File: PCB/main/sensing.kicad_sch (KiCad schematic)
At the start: 6 parts

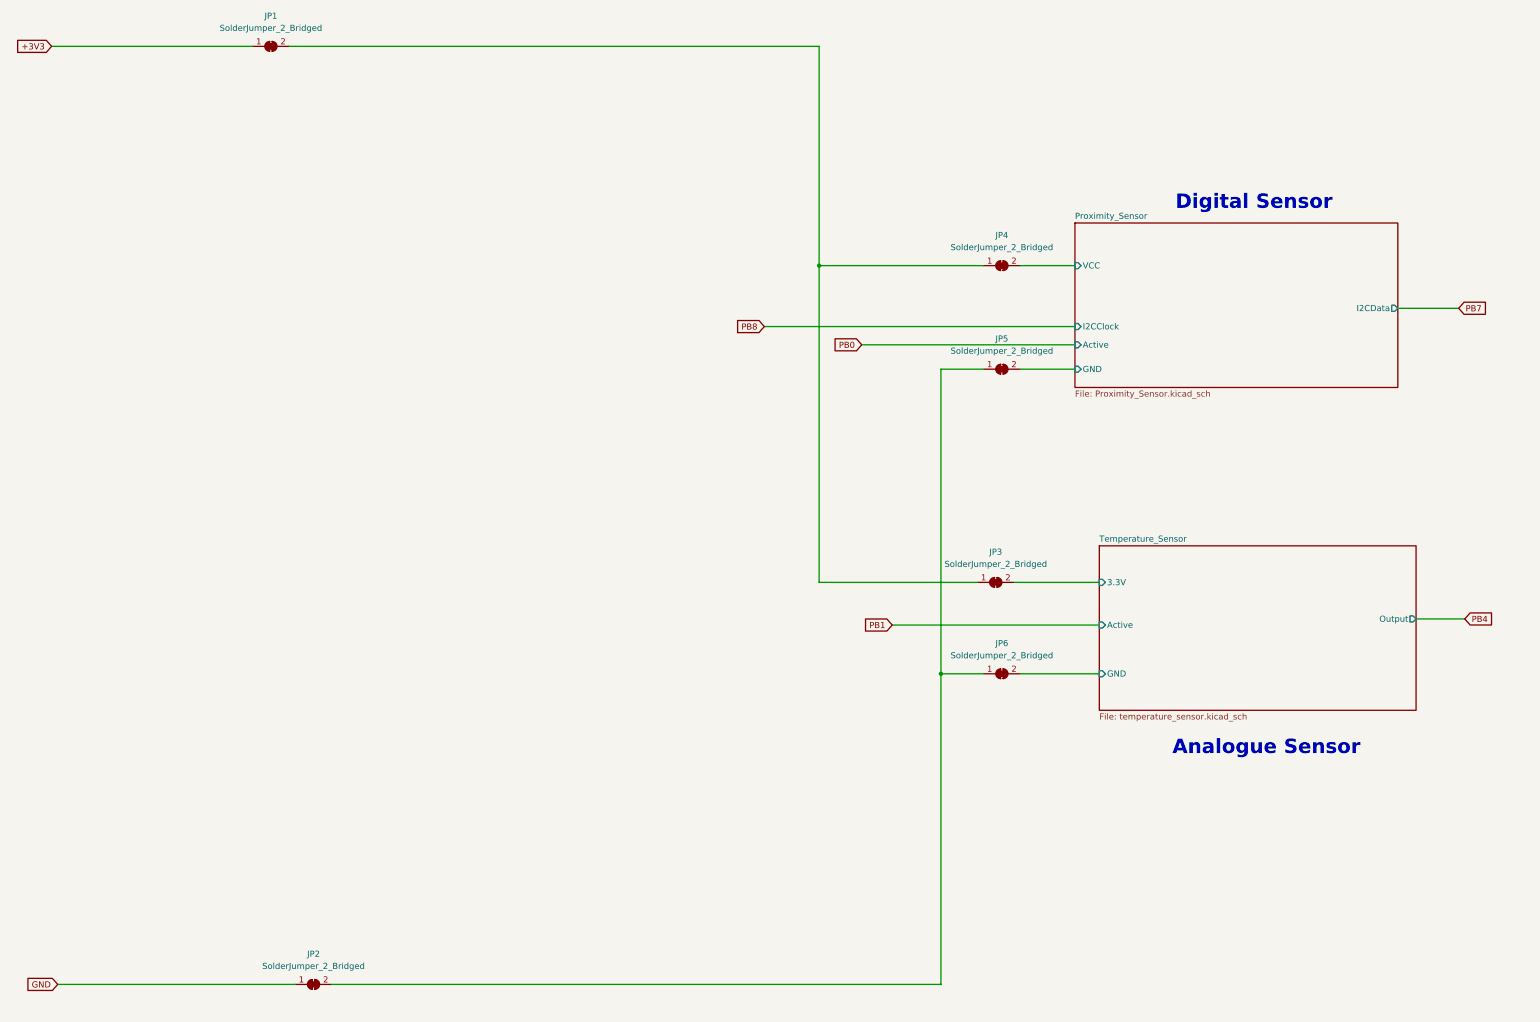
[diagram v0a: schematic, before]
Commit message: Correct labels
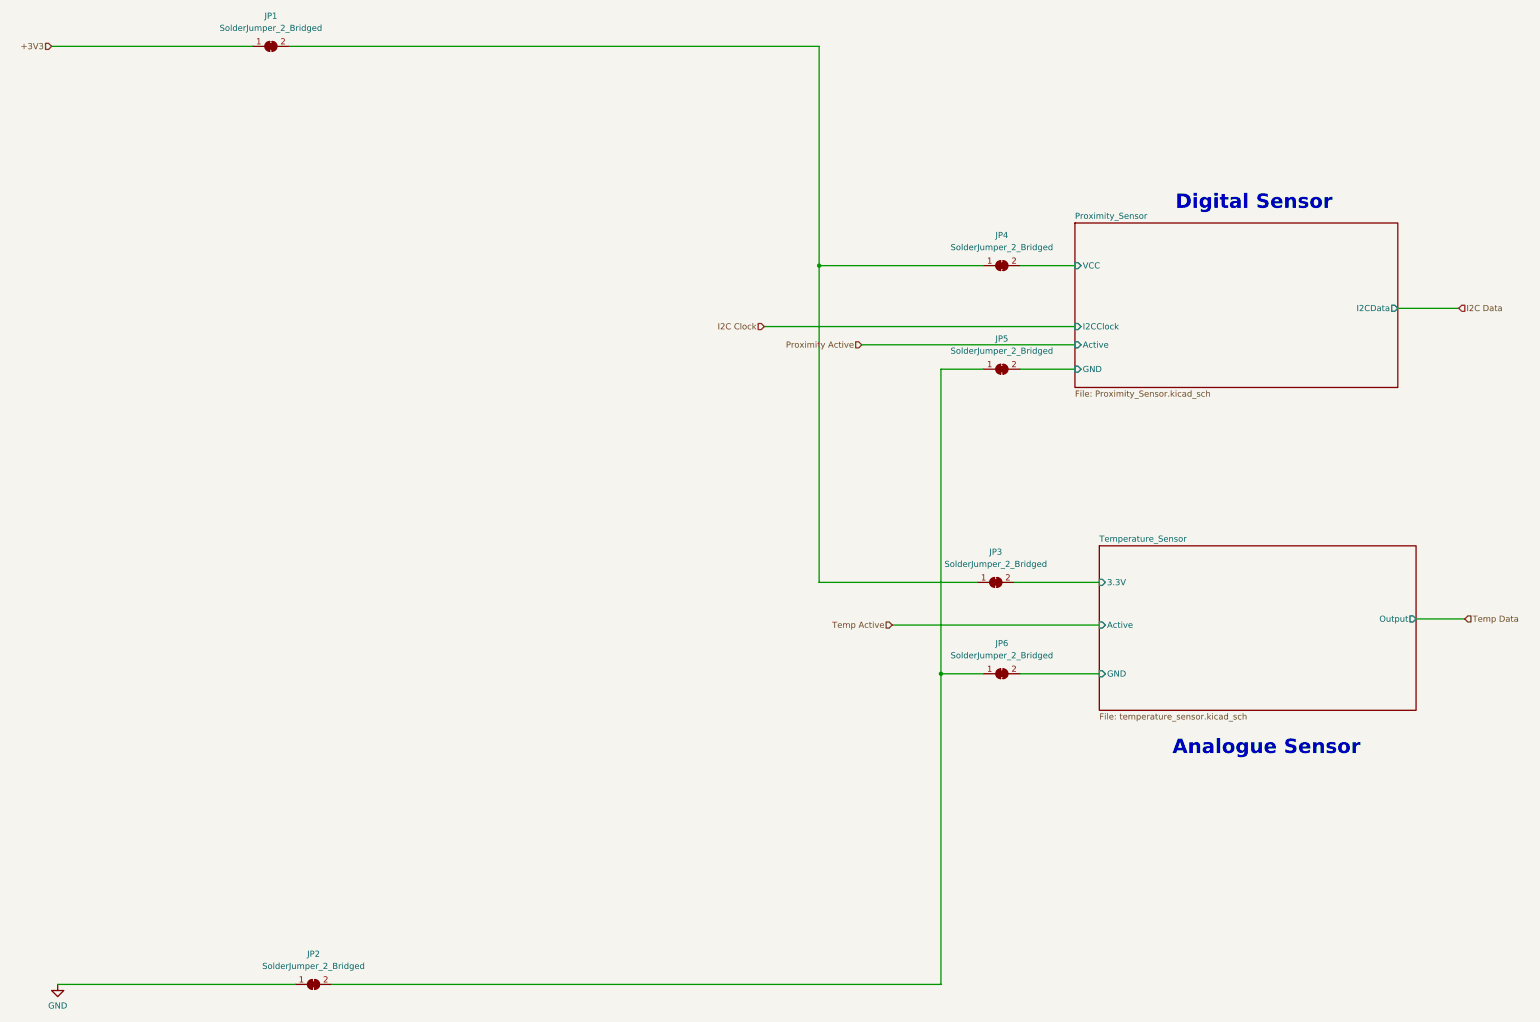
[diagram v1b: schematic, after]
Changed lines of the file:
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@@
     (effects (font (size 3 3) (thickness 0.6) bold) (justify left bottom))
   )
-  (global_label "PB8" (shape input) (at 185.42 105.41 180) (fields_autoplaced)
+  (hierarchical_label "Temp Data" (shape input) (at 331.47 166.37 0)
+    (effects (font (size 1.27 1.27)) (justify left))
+  )
+  (hierarchical_label "I2C Clock" (shape input) (at 185.42 105.41 180)
     (effects (font (size 1.27 1.27)) (justify right))
-    (property "Intersheet References" "${INTERSHEET_REFS}" (id 0) (at 179.2574 105.3306 0)
-      (effects (font (size 1.27 1.27)) (justify right) hide)
+  )
+  (hierarchical_label "Temp Active" (shape input) (at 212.09 167.64 180)
+    (effects (font (size 1.27 1.27)) (justify right))
+  )
+  (hierarchical_label "Proximity Active" (shape input) (at 205.74 109.22 180)
+    (effects (font (size 1.27 1.27)) (justify right))
+  )
+  (hierarchical_label "I2C Data" (shape input) (at 330.2 101.6 0)
+    (effects (font (size 1.27 1.27)) (justify left))
+  )
+  (hierarchical_label "+3V3" (shape input) (at 36.83 46.99 180)
+    (effects (font (size 1.27 1.27)) (justify right))
+  )
+  (symbol (lib_id "power:GND") (at 38.1 242.57 0) (unit 1)
+    (in_bom yes) (on_board yes) (fields_autoplaced)
+    (property "Reference" "#PWR024" (id 0) (at 38.1 248.92 0)
+      (effects (font (size 1.27 1.27)) hide)
     )
-  )
-  (global_label "PB7" (shape input) (at 330.2 101.6 0) (fields_autoplaced)
-    (effects (font (size 1.27 1.27)) (justify left))
-    (property "Intersheet References" "${INTERSHEET_REFS}" (id 0) (at 336.3626 101.5206 0)
-      (effects (font (size 1.27 1.27)) (justify left) hide)
+    (property "Value" "GND" (id 1) (at 38.1 247.0134 0))
+    (property "Footprint" "" (id 2) (at 38.1 242.57 0)
+      (effects (font (size 1.27 1.27)) hide)
     )
-  )
-  (global_label "+3V3" (shape input) (at 36.83 46.99 180) (fields_autoplaced)
-    (effects (font (size 1.27 1.27)) (justify right))
-    (property "Intersheet References" "${INTERSHEET_REFS}" (id 0) (at 29.3369 46.9106 0)
-      (effects (font (size 1.27 1.27)) (justify right) hide)
+    (property "Datasheet" "" (id 3) (at 38.1 242.57 0)
+      (effects (font (size 1.27 1.27)) hide)
     )
-  )
-  (global_label "GND" (shape input) (at 38.1 242.57 180) (fields_autoplaced)
-    (effects (font (size 1.27 1.27)) (justify right))
-    (property "Intersheet References" "${INTERSHEET_REFS}" (id 0) (at 31.8164 242.4906 0)
-      (effects (font (size 1.27 1.27)) (justify right) hide)
-    )
-  )
-  (global_label "PB4" (shape input) (at 331.47 166.37 0) (fields_autoplaced)
-    (effects (font (size 1.27 1.27)) (justify left))
-    (property "Intersheet References" "${INTERSHEET_REFS}" (id 0) (at 337.6326 166.2906 0)
-      (effects (font (size 1.27 1.27)) (justify left) hide)
-    )
-  )
-  (global_label "PB0" (shape input) (at 205.74 109.22 180) (fields_autoplaced)
-    (effects (font (size 1.27 1.27)) (justify right))
-    (property "Intersheet References" "${INTERSHEET_REFS}" (id 0) (at 199.5774 109.2994 0)
-      (effects (font (size 1.27 1.27)) (justify right) hide)
-    )
-  )
-  (global_label "PB1" (shape input) (at 212.09 167.64 180) (fields_autoplaced)
-    (effects (font (size 1.27 1.27)) (justify right))
-    (property "Intersheet References" "${INTERSHEET_REFS}" (id 0) (at 205.9274 167.7194 0)
-      (effects (font (size 1.27 1.27)) (justify right) hide)
-    )
+    (pin "1")
   )
   (symbol (lib_id "Jumper:SolderJumper_2_Bridged") (at 234.95 92.71 0) (unit 1)

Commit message: Work on reducing ERC flags
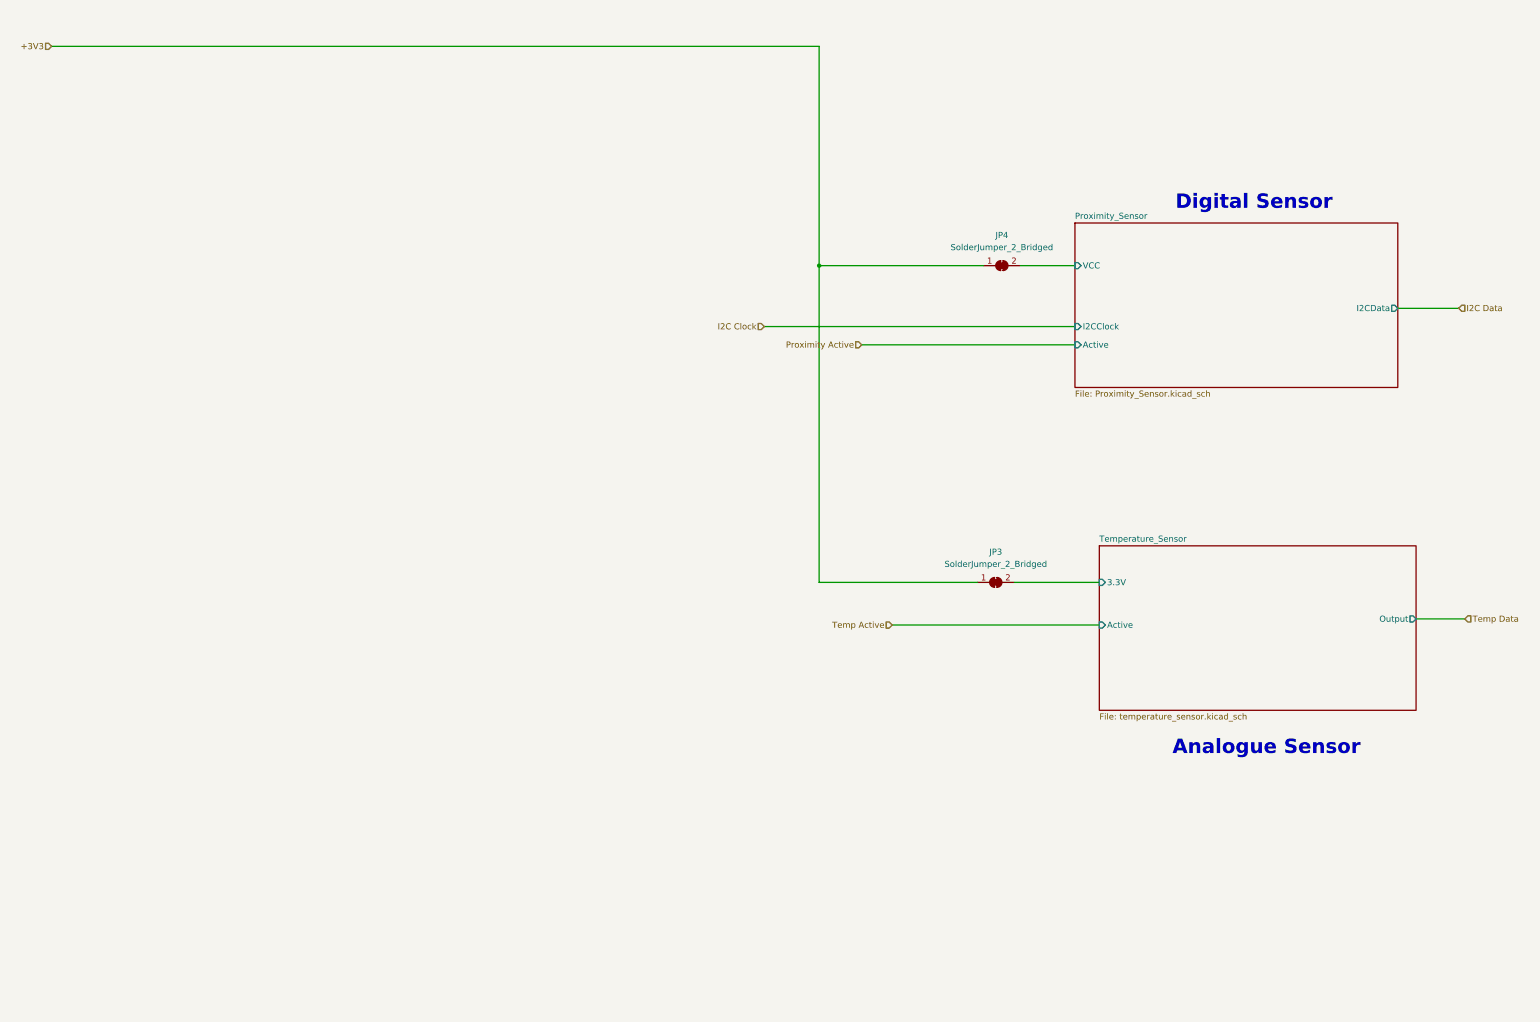
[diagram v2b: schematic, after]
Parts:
- removed JP1, JP2, JP5, JP6: SolderJumper_2_Bridged, symbol Jumper:SolderJumper_2_Bridged
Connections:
- net +3V3: now also JP3.1 (A), JP4.1 (A)
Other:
- sheet Proximity_Sensor ports: added none; removed GND
- sheet Temperature_Sensor ports: added none; removed GND
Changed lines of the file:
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@@
     (comment 4 "Authors: Kelvin Yankey")
-  )
-  (junction (at 222.25 177.8) (diameter 0) (color 0 0 0 0)
   )
   (junction (at 196.85 92.71) (diameter 0) (color 0 0 0 0)
   )
   (wire (pts (xy 321.31 166.37) (xy 331.47 166.37))
-    (stroke (width 0) (type default) (color 0 0 0 0))
-  )
-  (wire (pts (xy 222.25 177.8) (xy 222.25 114.3))
-    (stroke (width 0) (type default) (color 0 0 0 0))
-  )
-  (wire (pts (xy 222.25 242.57) (xy 222.25 177.8))
-    (stroke (width 0) (type default) (color 0 0 0 0))
-  )
-  (wire (pts (xy 238.76 177.8) (xy 255.27 177.8))
     (stroke (width 0) (type default) (color 0 0 0 0))
   )
@@
     (stroke (width 0) (type default) (color 0 0 0 0))
   )
-  (wire (pts (xy 86.36 46.99) (xy 196.85 46.99))
-    (stroke (width 0) (type default) (color 0 0 0 0))
-  )
   (wire (pts (xy 196.85 158.75) (xy 196.85 92.71))
     (stroke (width 0) (type default) (color 0 0 0 0))
   )
-  (wire (pts (xy 36.83 46.99) (xy 78.74 46.99))
+  (wire (pts (xy 36.83 46.99) (xy 196.85 46.99))
     (stroke (width 0) (type default) (color 0 0 0 0))
   )
   (wire (pts (xy 229.87 158.75) (xy 196.85 158.75))
-    (stroke (width 0) (type default) (color 0 0 0 0))
-  )
-  (wire (pts (xy 38.1 242.57) (xy 87.63 242.57))
-    (stroke (width 0) (type default) (color 0 0 0 0))
-  )
-  (wire (pts (xy 222.25 114.3) (xy 231.14 114.3))
     (stroke (width 0) (type default) (color 0 0 0 0))
   )
@@
     (stroke (width 0) (type default) (color 0 0 0 0))
   )
-  (wire (pts (xy 95.25 242.57) (xy 222.25 242.57))
-    (stroke (width 0) (type default) (color 0 0 0 0))
-  )
-  (wire (pts (xy 222.25 177.8) (xy 231.14 177.8))
-    (stroke (width 0) (type default) (color 0 0 0 0))
-  )
   (wire (pts (xy 196.85 92.71) (xy 231.14 92.71))
     (stroke (width 0) (type default) (color 0 0 0 0))
   )
   (wire (pts (xy 205.74 109.22) (xy 250.19 109.22))
-    (stroke (width 0) (type default) (color 0 0 0 0))
-  )
-  (wire (pts (xy 238.76 114.3) (xy 250.19 114.3))
     (stroke (width 0) (type default) (color 0 0 0 0))
   )
@@
     (effects (font (size 1.27 1.27)) (justify right))
   )
-  (symbol (lib_id "power:GND") (at 38.1 242.57 0) (unit 1)
-    (in_bom yes) (on_board yes) (fields_autoplaced)
-    (property "Reference" "#PWR024" (id 0) (at 38.1 248.92 0)
-      (effects (font (size 1.27 1.27)) hide)
-    )
-    (property "Value" "GND" (id 1) (at 38.1 247.0134 0))
-    (property "Footprint" "" (id 2) (at 38.1 242.57 0)
-      (effects (font (size 1.27 1.27)) hide)
-    )
-    (property "Datasheet" "" (id 3) (at 38.1 242.57 0)
-      (effects (font (size 1.27 1.27)) hide)
-    )
-    (pin "1")
-  )
   (symbol (lib_id "Jumper:SolderJumper_2_Bridged") (at 234.95 92.71 0) (unit 1)
     (in_bom yes) (on_board yes) (fields_autoplaced)
@@
     (pin "2")
   )
-  (symbol (lib_id "Jumper:SolderJumper_2_Bridged") (at 234.95 177.8 0) (unit 1)
-    (in_bom yes) (on_board yes) (fields_autoplaced)
-    (property "Reference" "JP6" (id 0) (at 234.95 171.45 0))
-    (property "Value" "SolderJumper_2_Bridged" (id 1) (at 234.95 173.99 0))
-    (property "Footprint" "" (id 2) (at 234.95 177.8 0)
-      (effects (font (size 1.27 1.27)) hide)
-    )
-    (property "Datasheet" "~" (id 3) (at 234.95 177.8 0)
-      (effects (font (size 1.27 1.27)) hide)
-    )
-    (pin "1")
-    (pin "2")
-  )
   (symbol (lib_id "Jumper:SolderJumper_2_Bridged") (at 233.68 158.75 0) (unit 1)
     (in_bom yes) (on_board yes) (fields_autoplaced)
@@
     )
     (property "Datasheet" "~" (id 3) (at 233.68 158.75 0)
-      (effects (font (size 1.27 1.27)) hide)
-    )
-    (pin "1")
-    (pin "2")
-  )
-  (symbol (lib_id "Jumper:SolderJumper_2_Bridged") (at 91.44 242.57 0) (unit 1)
-    (in_bom yes) (on_board yes) (fields_autoplaced)
-    (property "Reference" "JP2" (id 0) (at 91.44 236.22 0))
-    (property "Value" "SolderJumper_2_Bridged" (id 1) (at 91.44 238.76 0))
-    (property "Footprint" "" (id 2) (at 91.44 242.57 0)
-      (effects (font (size 1.27 1.27)) hide)
-    )
-    (property "Datasheet" "~" (id 3) (at 91.44 242.57 0)
-      (effects (font (size 1.27 1.27)) hide)
-    )
-    (pin "1")
-    (pin "2")
-  )
-  (symbol (lib_id "Jumper:SolderJumper_2_Bridged") (at 234.95 114.3 0) (unit 1)
-    (in_bom yes) (on_board yes) (fields_autoplaced)
-    (property "Reference" "JP5" (id 0) (at 234.95 107.95 0))
-    (property "Value" "SolderJumper_2_Bridged" (id 1) (at 234.95 110.49 0))
-    (property "Footprint" "" (id 2) (at 234.95 114.3 0)
-      (effects (font (size 1.27 1.27)) hide)
-    )
-    (property "Datasheet" "~" (id 3) (at 234.95 114.3 0)
-      (effects (font (size 1.27 1.27)) hide)
-    )
-    (pin "1")
-    (pin "2")
-  )
-  (symbol (lib_id "Jumper:SolderJumper_2_Bridged") (at 82.55 46.99 0) (unit 1)
-    (in_bom yes) (on_board yes) (fields_autoplaced)
-    (property "Reference" "JP1" (id 0) (at 82.55 40.64 0))
-    (property "Value" "SolderJumper_2_Bridged" (id 1) (at 82.55 43.18 0))
-    (property "Footprint" "" (id 2) (at 82.55 46.99 0)
-      (effects (font (size 1.27 1.27)) hide)
-    )
-    (property "Datasheet" "~" (id 3) (at 82.55 46.99 0)
       (effects (font (size 1.27 1.27)) hide)
     )
@@
       (effects (font (size 1.27 1.27)) (justify left))
     )
-    (pin "GND" input (at 250.19 114.3 180)
-      (effects (font (size 1.27 1.27)) (justify left))
-    )
     (pin "I2CClock" input (at 250.19 105.41 180)
       (effects (font (size 1.27 1.27)) (justify left))
@@
       (effects (font (size 1.27 1.27)) (justify left top))
     )
-    (pin "GND" input (at 255.27 177.8 180)
-      (effects (font (size 1.27 1.27)) (justify left))
-    )
     (pin "Output" output (at 321.31 166.37 0)

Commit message: Add footprints
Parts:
- JP3, JP4: footprint (none) -> Jumper:SolderJumper-2_P1.3mm_Bridged2Bar_Pad1.0x1.5mm
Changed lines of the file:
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@@
     (property "Reference" "JP4" (id 0) (at 234.95 86.36 0))
     (property "Value" "SolderJumper_2_Bridged" (id 1) (at 234.95 88.9 0))
-    (property "Footprint" "" (id 2) (at 234.95 92.71 0)
+    (property "Footprint" "Jumper:SolderJumper-2_P1.3mm_Bridged2Bar_Pad1.0x1.5mm" (id 2) (at 234.95 92.71 0)
       (effects (font (size 1.27 1.27)) hide)
     )
@@
     (property "Reference" "JP3" (id 0) (at 233.68 152.4 0))
     (property "Value" "SolderJumper_2_Bridged" (id 1) (at 233.68 154.94 0))
-    (property "Footprint" "" (id 2) (at 233.68 158.75 0)
+    (property "Footprint" "Jumper:SolderJumper-2_P1.3mm_Bridged2Bar_Pad1.0x1.5mm" (id 2) (at 233.68 158.75 0)
       (effects (font (size 1.27 1.27)) hide)
     )
